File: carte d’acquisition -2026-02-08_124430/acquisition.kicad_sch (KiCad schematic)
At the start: 34 parts, among them SW1 CK_KMS2xxG, SW2 BOOT, U1 STM32H747IITx, Y1 Crystal, Y2 Crystal

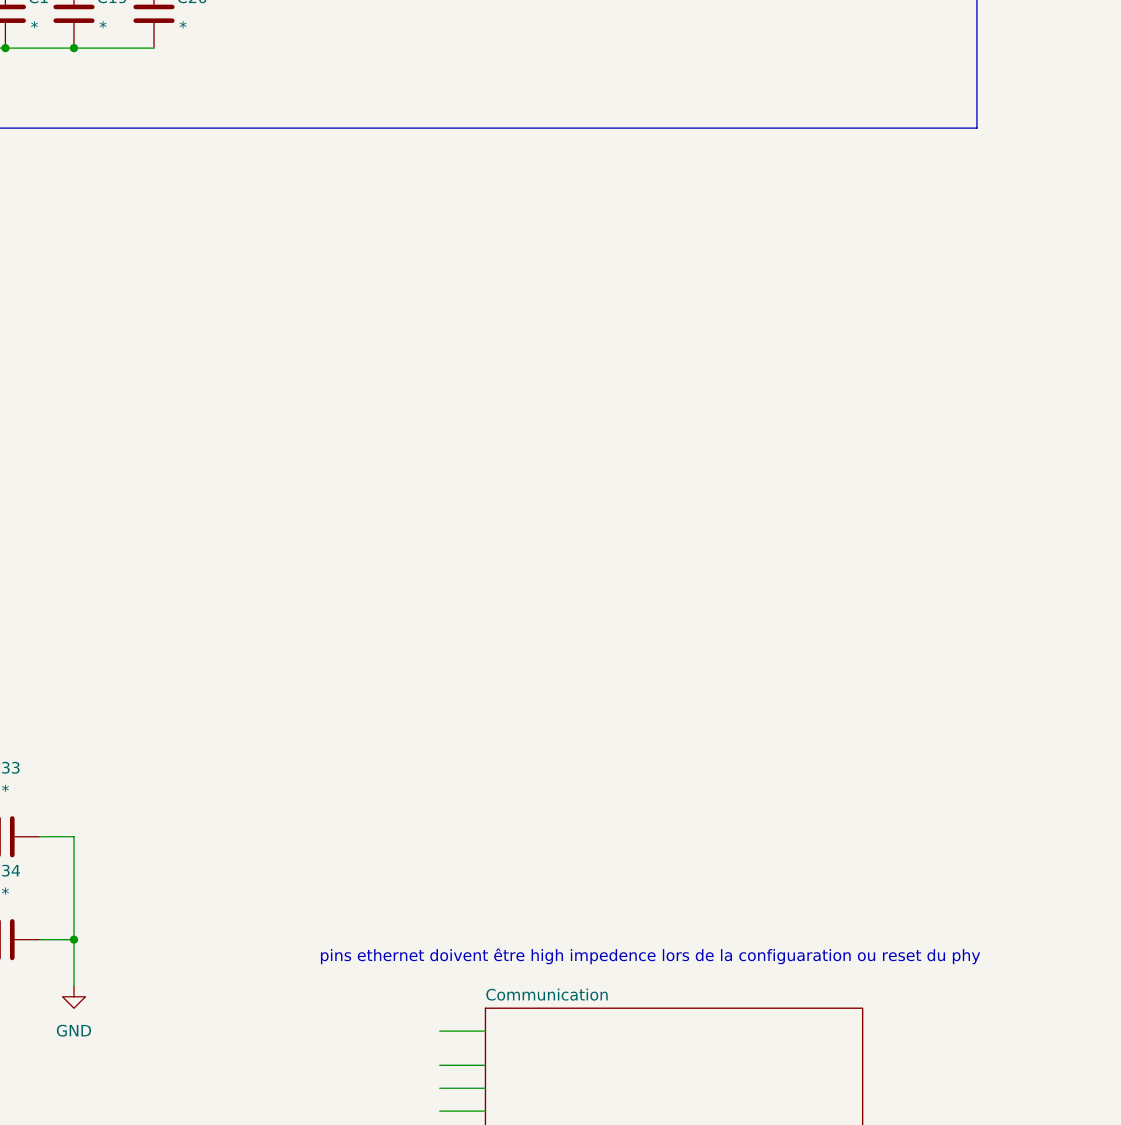
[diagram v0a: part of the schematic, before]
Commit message: Update acquisition.kicad_sch
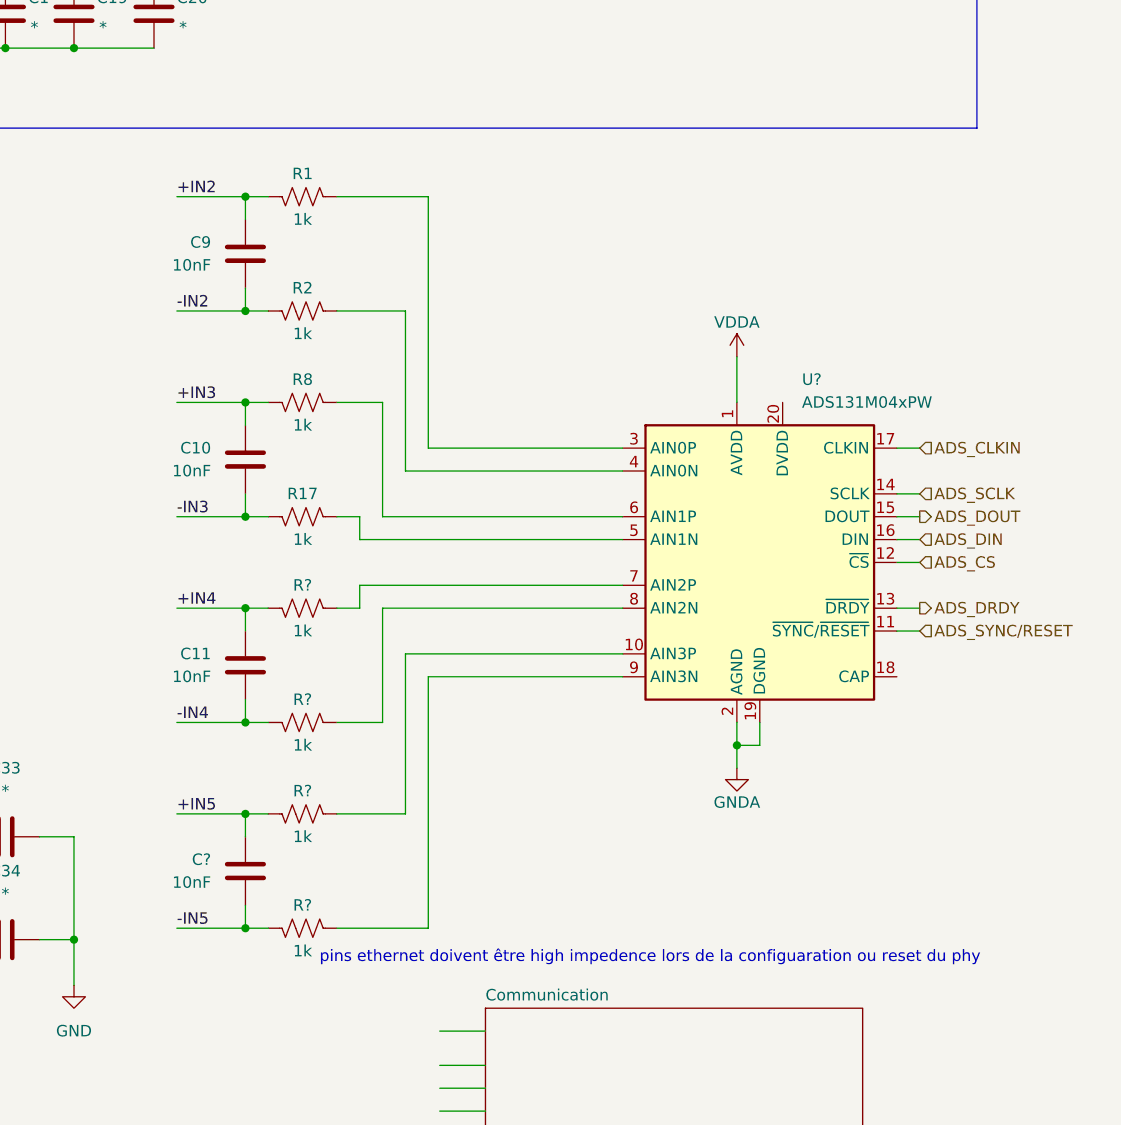
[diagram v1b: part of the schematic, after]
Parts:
- added C10, C11, C9, C?: 10nF, symbol Device:C
- added R1, R17, R2, R8, R? (x4): 1k, symbol Device:R_US
- added U?: ADS131M04xPW, Package_SO:TSSOP-20_4.4x6.5mm_P0.65mm, symbol Analog_ADC:ADS131M04xPW
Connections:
- new net: R?.1, U?.10 (AIN3P)
- new net: R17.1, U?.5 (AIN1N)
- new net: R?.1, U?.8 (AIN2N)
- new net: R1.1, U?.3 (AIN0P)
- new net: R2.1, U?.4 (AIN0N)
- new net: R8.1, U?.6 (AIN1P)
- new net: R?.1, U?.7 (AIN2P)
- new net: R?.1, U?.9 (AIN3N)
- new net +IN2: C9.2, R1.2
- new net +IN3: C10.2, R8.2
- new net +IN4: C11.2, R?.2
- new net +IN5: C?.2, R?.2
- new net -IN2: C9.1, R2.2
- new net -IN3: C10.1, R17.2
- new net -IN4: C11.1, R?.2
- new net -IN5: C?.1, R?.2
- new net ADS_CLKIN: U?.17 (CLKIN)
- new net ADS_CS: U?.12 (~{CS})
- new net ADS_DIN: U?.16 (DIN)
- new net ADS_DOUT: U?.15 (DOUT)
- new net ADS_DRDY: U?.13 (~{DRDY})
- new net ADS_SCLK: U?.14 (SCLK)
- new net ADS_SYNC/RESET: U?.11 (~{SYNC}/~{RESET})
- new net GNDA: U?.19 (DGND), U?.2 (AGND)
- new net VDDA: U?.1 (AVDD)

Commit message: Ajout clock et alim
Ajout de la clock et l'alim mais sans les schéma. Juste les fils
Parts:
- added U4: MIC5365-3.3YD5, Package_TO_SOT_SMD:TSOT-23-5, symbol Regulator_Linear:MIC5365-3.3YD5
- added Y3: ASCO, Oscillator:Oscillator_SMD_Abracon_ASCO-4Pin_1.6x1.2mm, symbol Oscillator:ASCO
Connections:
- net VDDA is gone; now on net 3V3A: U?.1 (AVDD)
- net 3V3A: now also U4.5 (VOUT)
- net GND: now also U4.2 (GND), Y3.2 (GND)
- net Out_Clock: now reaches U?.18 (CAP)
- net Out_Clock: now also Y3.3 (OUT)
- net 3V3D: now reaches U?.20 (DVDD)
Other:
- note added: "Buck pour 3V3D"
- note added: "Clock"
- note added: "LDO"
- note removed: "pins ethernet doivent être high impedence lors de la configuaration ou reset du phy"

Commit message: Feuille de plus et modifs de l'alim
J'ai ajouté une feuille pour le power et j'ai modifié les ldos et le buck mais il faut repasser dessus
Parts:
- removed U4: MIC5365-3.3YD5, Package_TO_SOT_SMD:TSOT-23-5, symbol Regulator_Linear:MIC5365-3.3YD5
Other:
- added sheet Power (power.kicad_sch)
- note removed: "Buck pour 3V3D"
- note removed: "LDO"
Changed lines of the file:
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@@
 		)
 	)
-	(text "Buck pour 3V3D"
-		(exclude_from_sim no)
-		(at 390.652 67.818 0)
-		(effects
-			(font
-				(size 1.27 1.27)
-			)
-		)
-	)
 	(text "Découplage"
 		(exclude_from_sim no)
@@
 		)
 	)
-	(text "LDO"
-		(exclude_from_sim no)
-		(at 355.854 64.008 0)
-		(effects
-			(font
-				(size 1.27 1.27)
-			)
-		)
-	)
 	(junction
 		(at 337.82 41.91)
@@
 	(wire
 		(pts
-			(xy 365.76 73.66) (xy 374.65 73.66)
-		)
-		(stroke
-			(width 0)
-			(type default)
-		)
-	)
-	(wire
-		(pts
 			(xy 331.47 134.62) (xy 328.93 134.62)
 		)
@@
 	(wire
 		(pts
-			(xy 383.54 116.84) (xy 383.54 121.92)
+			(xy 383.54 114.3) (xy 383.54 121.92)
 		)
 		(stroke
@@
 	(wire
 		(pts
-			(xy 389.89 77.47) (xy 405.13 77.47)
-		)
-		(stroke
-			(width 0)
-			(type default)
-		)
-	)
-	(wire
-		(pts
 			(xy 212.09 36.83) (xy 212.09 43.18)
 		)
@@
 		)
 	)
-	(label "3V3A"
-		(at 374.65 73.66 180)
-		(effects
-			(font
-				(size 1.27 1.27)
-			)
-			(justify right bottom)
-		)
-	)
 	(label "+IN4"
 		(at 321.31 144.78 0)
@@
 		)
 	)
-	(label "3V3A"
-		(at 383.54 116.84 180)
-		(effects
-			(font
-				(size 1.27 1.27)
-			)
-			(justify right bottom)
-		)
-	)
 	(label "+IN5"
 		(at 321.31 167.64 0)
@@
 		)
 	)
-	(label "3V3D"
-		(at 388.62 116.84 0)
-		(effects
-			(font
-				(size 1.27 1.27)
-			)
-			(justify left bottom)
-		)
-	)
 	(label "VDD33_USB"
 		(at 229.87 24.13 0)
@@
 		)
 	)
-	(label "3V3D"
-		(at 405.13 77.47 180)
-		(effects
-			(font
-				(size 1.27 1.27)
-			)
-			(justify right bottom)
-		)
-	)
 	(label "SD.CMD"
 		(at 269.24 187.96 0)
@@
 	)
 	(symbol
-		(lib_id "Regulator_Linear:MIC5365-3.3YD5")
-		(at 355.6 76.2 0)
-		(unit 1)
-		(exclude_from_sim no)
-		(in_bom yes)
-		(on_board yes)
-		(dnp no)
-		(fields_autoplaced yes)
-		(property "Reference" "U4"
-			(at 355.6 66.04 0)
-			(effects
-				(font
-					(size 1.27 1.27)
-				)
-			)
-		)
-		(property "Value" "MIC5365-3.3YD5"
-			(at 355.6 68.58 0)
-			(effects
-				(font
-					(size 1.27 1.27)
-				)
-			)
-		)
-		(property "Footprint" "Package_TO_SOT_SMD:TSOT-23-5"
-			(at 355.6 64.77 0)
-			(effects
-				(font
-					(size 1.27 1.27)
-				)
-				(hide yes)
-			)
-		)
-		(property "Datasheet" "https://ww1.microchip.com/downloads/aemDocuments/documents/APID/ProductDocuments/DataSheets/MIC5365-6-High-Performance-Single-150mA-LDO-DS20006605A.pdf"
-			(at 355.6 67.31 0)
-			(effects
-				(font
-					(size 1.27 1.27)
-				)
-				(hide yes)
-			)
-		)
-		(property "Description" "150mA Low-dropout Voltage Regulator, Vout 3.3V, Vin up to 5.5V, TSOT-23-5"
-			(at 355.6 62.23 0)
-			(effects
-				(font
-					(size 1.27 1.27)
-				)
-				(hide yes)
-			)
-		)
-		(pin "1"
-		)
-		(pin "5"
-		)
-		(pin "2"
-		)
-		(pin "4"
-		)
-		(pin "3"
-		)
-		(instances
-			(project ""
-				(path "/eaacffe0-ee57-428e-a37e-5655e0922ccc"
-					(reference "U4")
-					(unit 1)
-				)
-			)
-		)
-	)
-	(symbol
 		(lib_id "Device:C")
 		(at 302.26 170.18 90)
@@
 	)
 	(symbol
-		(lib_id "power:GND")
-		(at 355.6 83.82 0)
-		(unit 1)
-		(exclude_from_sim no)
-		(in_bom yes)
-		(on_board yes)
-		(dnp no)
-		(fields_autoplaced yes)
-		(property "Reference" "#PWR08"
-			(at 355.6 90.17 0)
-			(effects
-				(font
-					(size 1.27 1.27)
-				)
-				(hide yes)
-			)
-		)
-		(property "Value" "GND"
-			(at 355.6 88.9 0)
-			(effects
-				(font
-					(size 1.27 1.27)
-				)
-			)
-		)
-		(property "Footprint" ""
-			(at 355.6 83.82 0)
-			(effects
-				(font
-					(size 1.27 1.27)
-				)
-				(hide yes)
-			)
-		)
-		(property "Datasheet" ""
-			(at 355.6 83.82 0)
-			(effects
-				(font
-					(size 1.27 1.27)
-				)
-				(hide yes)
-			)
-		)
-		(property "Description" "Power symbol creates a global label with name \"GND\" , ground"
-			(at 355.6 83.82 0)
-			(effects
-				(font
-					(size 1.27 1.27)
-				)
-				(hide yes)
-			)
-		)
-		(pin "1"
-		)
-		(instances
-			(project "acquisition"
-				(path "/eaacffe0-ee57-428e-a37e-5655e0922ccc"
-					(reference "#PWR08")
-					(unit 1)
-				)
-			)
-		)
-	)
-	(symbol
 		(lib_id "Device:C")
 		(at 307.34 45.72 0)
@@
 	)
 	(symbol
+		(lib_id "power:+3.3VA")
+		(at 383.54 114.3 0)
+		(unit 1)
+		(exclude_from_sim no)
+		(in_bom yes)
+		(on_board yes)
+		(dnp no)
+		(property "Reference" "#PWR023"
+			(at 383.54 118.11 0)
+			(effects
+				(font
+					(size 1.27 1.27)
+				)
+				(hide yes)
+			)
+		)
+		(property "Value" "3V3A"
+			(at 383.54 109.22 0)
+			(effects
+				(font
+					(size 1.27 1.27)
+				)
+			)
+		)
+		(property "Footprint" ""
+			(at 383.54 114.3 0)
+			(effects
+				(font
+					(size 1.27 1.27)
+				)
+				(hide yes)
+			)
+		)
+		(property "Datasheet" ""
+			(at 383.54 114.3 0)
+			(effects
+				(font
+					(size 1.27 1.27)
+				)
+				(hide yes)
+			)
+		)
+		(property "Description" "Power symbol creates a global label with name \"+3.3VA\""
+			(at 383.54 114.3 0)
+			(effects
+				(font
+					(size 1.27 1.27)
+				)
+				(hide yes)
+			)
+		)
+		(pin "1"
+		)
+		(instances
+			(project ""
+				(path "/eaacffe0-ee57-428e-a37e-5655e0922ccc"
+					(reference "#PWR023")
+					(unit 1)
+				)
+			)
+		)
+	)
+	(symbol
 		(lib_id "0CSL_D1_V1:Battery_Holder_1025")
 		(at 171.45 25.4 270)
@@
 	)
 	(symbol
+		(lib_id "power:+3.3VA")
+		(at 388.62 116.84 0)
+		(unit 1)
+		(exclude_from_sim no)
+		(in_bom yes)
+		(on_board yes)
+		(dnp no)
+		(fields_autoplaced yes)
+		(property "Reference" "#PWR032"
+			(at 388.62 120.65 0)
+			(effects
+				(font
+					(size 1.27 1.27)
+				)
+				(hide yes)
+			)
+		)
+		(property "Value" "3V3D"
+			(at 388.62 111.76 0)
+			(effects
+				(font
+					(size 1.27 1.27)
+				)
+			)
+		)
+		(property "Footprint" ""
+			(at 388.62 116.84 0)
+			(effects
+				(font
+					(size 1.27 1.27)
+				)
+				(hide yes)
+			)
+		)
+		(property "Datasheet" ""
+			(at 388.62 116.84 0)
+			(effects
+				(font
+					(size 1.27 1.27)
+				)
+				(hide yes)
+			)
+		)
+		(property "Description" "Power symbol creates a global label with name \"+3.3VA\""
+			(at 388.62 116.84 0)
+			(effects
+				(font
+					(size 1.27 1.27)
+				)
+				(hide yes)
+			)
+		)
+		(pin "1"
+		)
+		(instances
+			(project ""
+				(path "/eaacffe0-ee57-428e-a37e-5655e0922ccc"
+					(reference "#PWR032")
+					(unit 1)
+				)
+			)
+		)
+	)
+	(symbol
 		(lib_id "power:GND")
 		(at 309.88 186.69 0)
@@
 				)
 			)
+		)
+	)
+	(sheet
+		(at 24.13 66.04)
+		(size 46.99 19.05)
+		(exclude_from_sim no)
+		(in_bom yes)
+		(on_board yes)
+		(dnp no)
+		(fields_autoplaced yes)
+		(stroke
+			(width 0.1524)
+			(type solid)
+		)
+		(fill
+			(color 0 0 0 0.0000)
+		)
+		(property "Sheetname" "Power"
+			(at 24.13 65.3284 0)
+			(effects
+				(font
+					(size 1.27 1.27)
+				)
+				(justify left bottom)
+			)
+		)
+		(property "Sheetfile" "power.kicad_sch"
+			(at 24.13 85.6746 0)
+			(effects
+				(font
+					(size 1.27 1.27)
+				)
+				(justify left top)
+			)
+		)
+		(instances
+			(project "acquisition"
+				(path "/eaacffe0-ee57-428e-a37e-5655e0922ccc"
+					(page "5")
+				)
+			)

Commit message: thermocouple
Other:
- added sheet thermocouple (thermocouple.kicad_sch)
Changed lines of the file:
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@@
+	)
+	(sheet
+		(at 24.13 30.48)
+		(size 48.26 25.4)
+		(exclude_from_sim no)
+		(in_bom yes)
+		(on_board yes)
+		(dnp no)
+		(fields_autoplaced yes)
+		(stroke
+			(width 0.1524)
+			(type solid)
+		)
+		(fill
+			(color 0 0 0 0.0000)
+		)
+		(property "Sheetname" "thermocouple"
+			(at 24.13 29.7684 0)
+			(effects
+				(font
+					(size 1.27 1.27)
+				)
+				(justify left bottom)
+			)
+		)
+		(property "Sheetfile" "thermocouple.kicad_sch"
+			(at 24.13 56.4646 0)
+			(effects
+				(font
+					(size 1.27 1.27)
+				)
+				(justify left top)
+			)
+		)
+		(instances
+			(project "acquisition"
+				(path "/eaacffe0-ee57-428e-a37e-5655e0922ccc"
+					(page "6")
+				)
+			)
+		)
 	)
 	(sheet

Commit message: Power et maj can et sd
Modifications sur l'alim selon le schéma sur Canvas et mise à jour du can et carte sd
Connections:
- net Out_Clock: no longer U?.18 (CAP)
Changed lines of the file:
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@@
 	(wire
 		(pts
+			(xy 146.05 62.23) (xy 146.05 63.5)
+		)
+		(stroke
+			(width 0)
+			(type default)
+		)
+	)
+	(wire
+		(pts
 			(xy 295.91 74.93) (xy 302.26 74.93)
 		)
@@
 	(wire
 		(pts
-			(xy 401.32 152.4) (xy 412.75 152.4)
+			(xy 135.89 38.1) (xy 139.7 38.1)
 		)
 		(stroke
@@
 	(wire
 		(pts
-			(xy 135.89 38.1) (xy 139.7 38.1)
+			(xy 330.2 41.91) (xy 337.82 41.91)
 		)
 		(stroke
@@
 	(wire
 		(pts
-			(xy 330.2 41.91) (xy 337.82 41.91)
+			(xy 219.71 36.83) (xy 217.17 36.83)
 		)
 		(stroke
@@
 	(wire
 		(pts
-			(xy 219.71 36.83) (xy 217.17 36.83)
+			(xy 153.67 66.04) (xy 163.83 66.04)
 		)
 		(stroke
@@
 	(wire
 		(pts
+			(xy 153.67 62.23) (xy 153.67 66.04)
+		)
+		(stroke
+			(width 0)
+			(type default)
+		)
+	)
+	(wire
+		(pts
 			(xy 179.07 25.4) (xy 181.61 25.4)
 		)
@@
 	(wire
 		(pts
-			(xy 153.67 66.04) (xy 163.83 66.04)
-		)
-		(stroke
-			(width 0)
-			(type default)
-		)
-	)
-	(wire
-		(pts
 			(xy 114.3 97.79) (xy 114.3 86.36)
 		)
@@
 		)
 	)
-	(label "Out_Clock"
-		(at 412.75 152.4 180)
-		(effects
-			(font
-				(size 1.27 1.27)
-			)
-			(justify right bottom)
-		)
-	)
 	(label "+IN3"
 		(at 321.31 121.92 0)
@@
 	(symbol
 		(lib_id "power:+3.3V")
-		(at 146.05 63.5 0)
+		(at 146.05 62.23 0)
 		(unit 1)
 		(exclude_from_sim no)
@@
 		(dnp no)
 		(property "Reference" "#PWR050"
-			(at 146.05 67.31 0)
+			(at 146.05 66.04 0)
 			(effects
 				(font
@@
 		)
 		(property "Value" "3V3"
-			(at 147.828 60.706 0)
+			(at 140.716 60.706 0)
 			(effects
 				(font
@@
 		)
 		(property "Footprint" ""
-			(at 146.05 63.5 0)
+			(at 146.05 62.23 0)
 			(effects
 				(font
@@
 		)
 		(property "Datasheet" ""
-			(at 146.05 63.5 0)
+			(at 146.05 62.23 0)
 			(effects
 				(font
@@
 		)
 		(property "Description" "Power symbol creates a global label with name \"+3.3V\""
-			(at 146.05 63.5 0)
+			(at 146.05 62.23 0)
 			(effects
 				(font
@@
 	(symbol
 		(lib_id "power:+3.3V")
-		(at 153.67 66.04 0)
+		(at 153.67 62.23 0)
 		(unit 1)
 		(exclude_from_sim no)
@@
 		(dnp no)
 		(property "Reference" "#PWR043"
-			(at 153.67 69.85 0)
+			(at 153.67 66.04 0)
 			(effects
 				(font
@@
 		)
 		(property "Value" "3V3A"
-			(at 155.448 63.246 0)
+			(at 154.94 60.96 0)
 			(effects
 				(font
@@
 		)
 		(property "Footprint" ""
-			(at 153.67 66.04 0)
+			(at 153.67 62.23 0)
 			(effects
 				(font
@@
 		)
 		(property "Datasheet" ""
-			(at 153.67 66.04 0)
+			(at 153.67 62.23 0)
 			(effects
 				(font
@@
 		)
 		(property "Description" "Power symbol creates a global label with name \"+3.3V\""
-			(at 153.67 66.04 0)
+			(at 153.67 62.23 0)
 			(effects
 				(font

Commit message: STM et ADS131 dans des feuilles
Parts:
- removed BT1: RTC_BAT, 0CSL_D1_V1:BatteryHolder_BHX1_1025, symbol 0CSL_D1_V1:Battery_Holder_1025
- removed C1, C14, C15, C16, C17, C18, C19, C2, C20, C3, C33, C34, C4, C5, C8: *, symbol Device:C
- removed C10, C11, C9, C?: 10nF, symbol Device:C
- removed C23, C24, C25, C31: 2.2u, symbol Device:C
- removed C26, C27: 6pF, symbol Device:C
- removed C32: 100n, symbol Device:C
- removed R1, R17, R2, R8, R? (x4): 1k, symbol Device:R_US
- removed R14, R39: 10k, symbol Device:R_US
- removed R15, R16, R40: 0, symbol Device:R_US
- removed R27: 100k, symbol Device:R_US
- removed SW1: CK_KMS2xxG, Button_Switch_SMD:SW_SPST_CK_KMS2xxGP, symbol Switch:CK_KMS2xxG
- removed SW2: BOOT, symbol Switch:SW_Push_SPDT
- removed U1: STM32H747IITx, Package_QFP:LQFP-176_24x24mm_P0.5mm, symbol MCU_ST_STM32H7:STM32H747IITx
- removed U?: ADS131M04xPW, Package_SO:TSSOP-20_4.4x6.5mm_P0.65mm, symbol Analog_ADC:ADS131M04xPW
- removed Y1, Y2: Crystal, Crystal:Crystal_SMD_3225-4Pin_3.2x2.5mm, symbol Device:Crystal
- removed Y3: ASCO, Oscillator:Oscillator_SMD_Abracon_ASCO-4Pin_1.6x1.2mm, symbol Oscillator:ASCO
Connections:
- no-connect marks 5 -> 0
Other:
- added sheet ADS131 (ADS131.kicad_sch)
- added sheet Microcontrolleur (microcontrolleur.kicad_sch)
- note removed: "Clock"
- note removed: "Découplage"

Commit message: arthur net
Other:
- sheet ADS131 ports: added ADS_CLKIN, ADS_CS, ADS_DIN, ADS_DOUT, ADS_DRDY, ADS_SCLK, ADS_SYNC/RESET; removed none
- sheet Communication ports: added CAN.FAULT, CAN.RXD, CAN.TXD; removed none
- sheet Microcontrolleur ports: added BC0, BC1, BC2, BC3, CAN.RXD, CAN.STBY, CAN.TXD, I2C1_SCL, I2C1_SDA, JTCK, JTDI, JTDO, JTMS, NJTRST, SD.CLK, SD.CMD, SD.DAT0, SD.DAT1, SD.DAT2, SD.DAT3, SD.DET, SPI1_MISO, SPI1_MOSI, SPI1_NSS, SPI1_SCK, SPI2_MISO, SPI2_MOSI, SPI2_NSS, SPI2_SCK, SPI4_MISO, SPI4_MOSI, SPI4_NSS, SPI4_SCK, SPI5_MISO, SPI5_MOSI, SPI5_NSS, SPI5_SCK; removed none
- sheet Power ports: added LED1, LED2, LED3, TPS3V5_INT, TPS3V5_SCL, TPS3V5_SDA; removed none
- sheet thermocouple ports: added ADS_CLKIN, ADS_CS, ADS_DIN, ADS_DOUT, ADS_DRDY, ADS_SCLK, ADS_SYNC/RESET, BC0, BC1, BC2, BC3, CS_10, CS_ref, MISO_10_T, MISO_ref_T, SCK_10, SCK_ref; removed none
- note added: "entre sortie ?"
- note added: "ques qui menque ?"
- note added: "sinonime ?"

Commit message: arthur
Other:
- sheet Microcontrolleur ports: added ADC_4theromocouple, ADS_loadcell, led0, led1, led2; removed none
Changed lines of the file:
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@@
+	(wire
+		(pts
+			(xy 59.69 66.04) (xy 59.69 62.23)
+		)
+		(stroke
+			(width 0)
+			(type default)
+		)
+	)
+	(wire
+		(pts
+			(xy 215.9 175.26) (xy 215.9 224.79)
+		)
+		(stroke
+			(width 0)
+			(type default)
+		)
+	)
 	(wire
 		(pts
@@
 	(wire
 		(pts
+			(xy 59.69 62.23) (xy 166.37 62.23)
+		)
+		(stroke
+			(width 0)
+			(type default)
+		)
+	)
+	(wire
+		(pts
 			(xy 240.03 138.43) (xy 252.73 138.43)
 		)
@@
 	(wire
 		(pts
+			(xy 54.61 66.04) (xy 54.61 57.15)
+		)
+		(stroke
+			(width 0)
+			(type default)
+		)
+	)
+	(wire
+		(pts
 			(xy 129.54 107.95) (xy 129.54 115.57)
 		)
@@
 	(wire
 		(pts
+			(xy 240.03 128.27) (xy 252.73 128.27)
+		)
+		(stroke
+			(width 0)
+			(type default)
+		)
+	)
+	(wire
+		(pts
 			(xy 240.03 123.19) (xy 252.73 123.19)
 		)
@@
 	(wire
 		(pts
+			(xy 166.37 62.23) (xy 166.37 66.04)
+		)
+		(stroke
+			(width 0)
+			(type default)
+		)
+	)
+	(wire
+		(pts
 			(xy 246.38 111.76) (xy 252.73 111.76)
 		)
@@
 	(wire
 		(pts
+			(xy 57.15 59.69) (xy 57.15 66.04)
+		)
+		(stroke
+			(width 0)
+			(type default)
+		)
+	)
+	(wire
+		(pts
+			(xy 168.91 59.69) (xy 57.15 59.69)
+		)
+		(stroke
+			(width 0)
+			(type default)
+		)
+	)
+	(wire
+		(pts
 			(xy 240.03 125.73) (xy 252.73 125.73)
 		)
@@
 	(wire
 		(pts
+			(xy 215.9 224.79) (xy 83.82 224.79)
+		)
+		(stroke
+			(width 0)
+			(type default)
+		)
+	)
+	(wire
+		(pts
 			(xy 240.03 140.97) (xy 252.73 140.97)
 		)
@@
 	(wire
 		(pts
+			(xy 171.45 57.15) (xy 171.45 66.04)
+		)
+		(stroke
+			(width 0)
+			(type default)
+		)
+	)
+	(wire
+		(pts
 			(xy 240.03 96.52) (xy 250.19 96.52)
 		)
@@
 	(wire
 		(pts
+			(xy 54.61 57.15) (xy 171.45 57.15)
+		)
+		(stroke
+			(width 0)
+			(type default)
+		)
+	)
+	(wire
+		(pts
 			(xy 134.62 110.49) (xy 163.83 110.49)
 		)
@@
 		(pts
 			(xy 250.19 93.98) (xy 252.73 93.98)
+		)
+		(stroke
+			(width 0)
+			(type default)
+		)
+	)
+	(wire
+		(pts
+			(xy 168.91 66.04) (xy 168.91 59.69)
 		)
 		(stroke
@@
 			(effects
 				(font
+					(size 1.27 1.27)
+				)
+				(justify right)
+			)
+		)
+		(pin "ADC_4theromocouple" output
+			(at 240.03 128.27 0)
+			(effects
+				(font
+					(size 1.27 1.27)
+				)
+				(justify right)
+			)
+		)
+		(pin "ADS_loadcell" output
+			(at 215.9 175.26 270)
+			(effects
+				(font
+					(size 1.27 1.27)
+				)
+				(justify left)
+			)
+		)
+		(pin "led0" output
+			(at 171.45 66.04 90)
+			(effects
+				(font
+					(size 1.27 1.27)
+				)
+				(justify right)
+			)
+		)
+		(pin "led1" output
+			(at 168.91 66.04 90)
+			(effects
+				(font
+					(size 1.27 1.27)
+				)
+				(justify right)
+			)
+		)
+		(pin "led2" output
+			(at 166.37 66.04 90)
+			(effects
+				(font
